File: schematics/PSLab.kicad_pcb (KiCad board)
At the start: 4 copper layers, 99 x 53.3 mm, 182 parts, among them J1 DoublePins, J11 Li-Ion Battery, J2 Power Pins, J3 Wave Generator, J4 I2C, J5 I2C, J6 ESP01, J7 UART, J9 SPI, P1 SDCard, Q1 MMBT3906, Q2 MMBT3904, Q3 MMBT3906, Q4 Q_NMOS_DGS, SW1 BOOT, SW2 MCLR Reset, SW3 USB_C - Generic, U1 LDFM33PUR, U10 TL082, U11 TL082, U12 MCP4728, U13 MCP6S21, U14 MCP6S21, U15 CP2102N, U16 SP0503BAHT, U18 LTC4040, U19 TC1240A, U2 74HC126, U3 PIC24EP256GP204, U4 DS1307Z+, U5 TC7660, U7 LM324, U8 TL082, U9 TL082, X2 32.768 kHz, Y1 12 MHz

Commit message: fix: osc signal routes
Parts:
- BT1: footprint Battery:BatteryHolder_LINX_BAT-HLD-012-SMT -> PSLab:BatteryHolder_LINX_BAT-HLD-012-SMT
- moved TP3 36.7 mm to (145.4, 66.3)
- moved TP2 35.6 mm to (148.7, 66.3)
- moved TP5 35.2 mm to (147.1, 68.6)
- moved TP1 30.4 mm to (152.2, 66.3)
- moved R24 19.9 mm to (180.4, 83.5)
- moved C25 16.0 mm to (180.4, 85.8), turned to 180 degrees
- moved U4 1.46 mm to (158.9, 104.9)
- moved X2 1.28 mm to (165.4, 107.0)
- moved R36 1.09 mm to (176.0, 83.5)
- moved C39 0.99 mm to (180.4, 94.0), turned to 180 degrees
- moved U13 0.95 mm to (178.2, 89.9)
- moved R22 0.78 mm to (176.0, 94.0), turned to 180 degrees
- moved R7 0.77 mm to (180.4, 98.3)
- moved R23 0.75 mm to (176.0, 85.8)
- moved R8 0.72 mm to (180.4, 96.2)
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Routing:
- net AVdd: track 109.0 -> 92.0 mm
- net AVSS: track 304.5 -> 290.5 mm, vias 29 -> 25
- net ACH1: track 12.0 -> 20.4 mm
- net CH1: track 17.6 -> 24.6 mm
- net Net-(BT1-Pad1): track 4.03 -> 1.91 mm
- net VDDA: track 6.73 -> 8.13 mm, vias 1 -> 0
- net LA4: track 8.02 -> 9.34 mm
- net CS.CH1: track 57.0 -> 57.9 mm
- net +5V: track 180.3 -> 179.5 mm, vias 10 -> 9
- net /LA2_: track 50.2 -> 51.0 mm
- net LA3: track 3.15 -> 3.84 mm
- net LA1: track 9.17 -> 9.78 mm
- net /LA3_: track 46.6 -> 47.2 mm
- net LA2: track 3.17 -> 3.68 mm

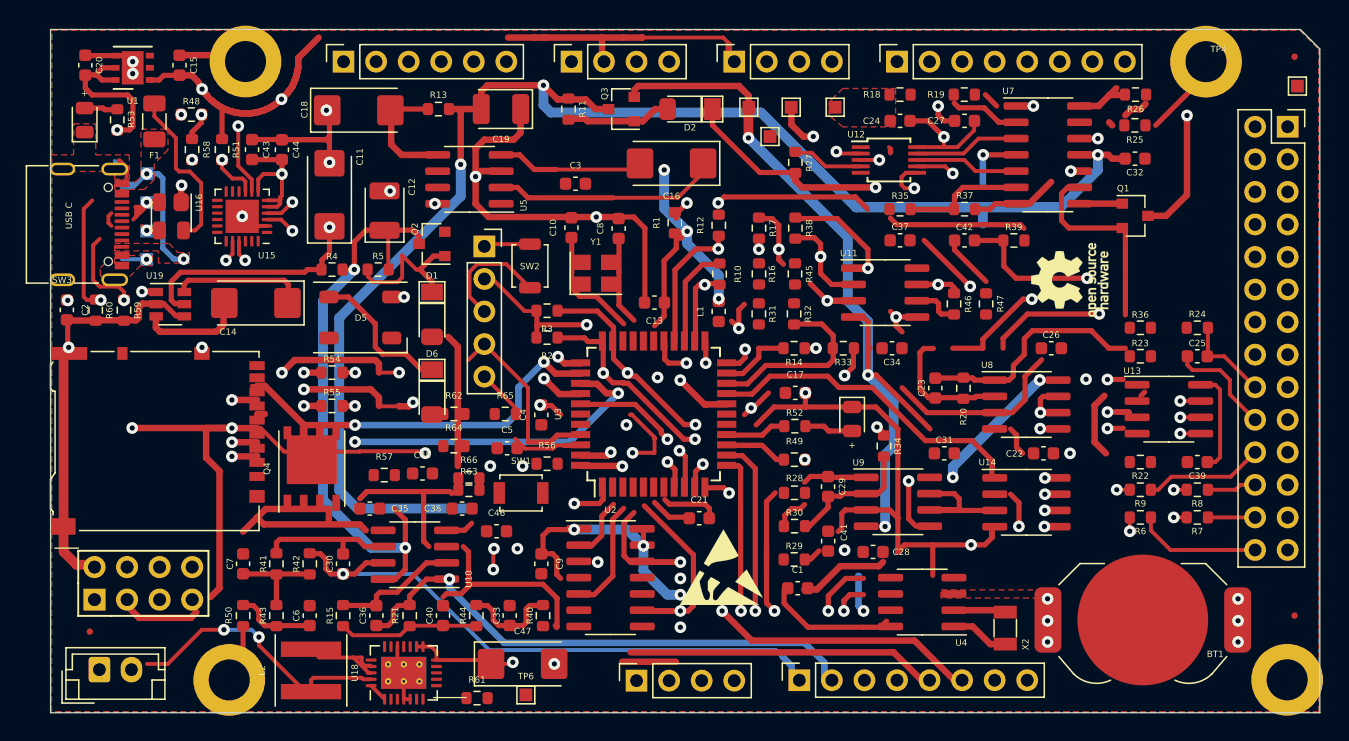
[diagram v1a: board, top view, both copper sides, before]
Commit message: refactor: global track refresh
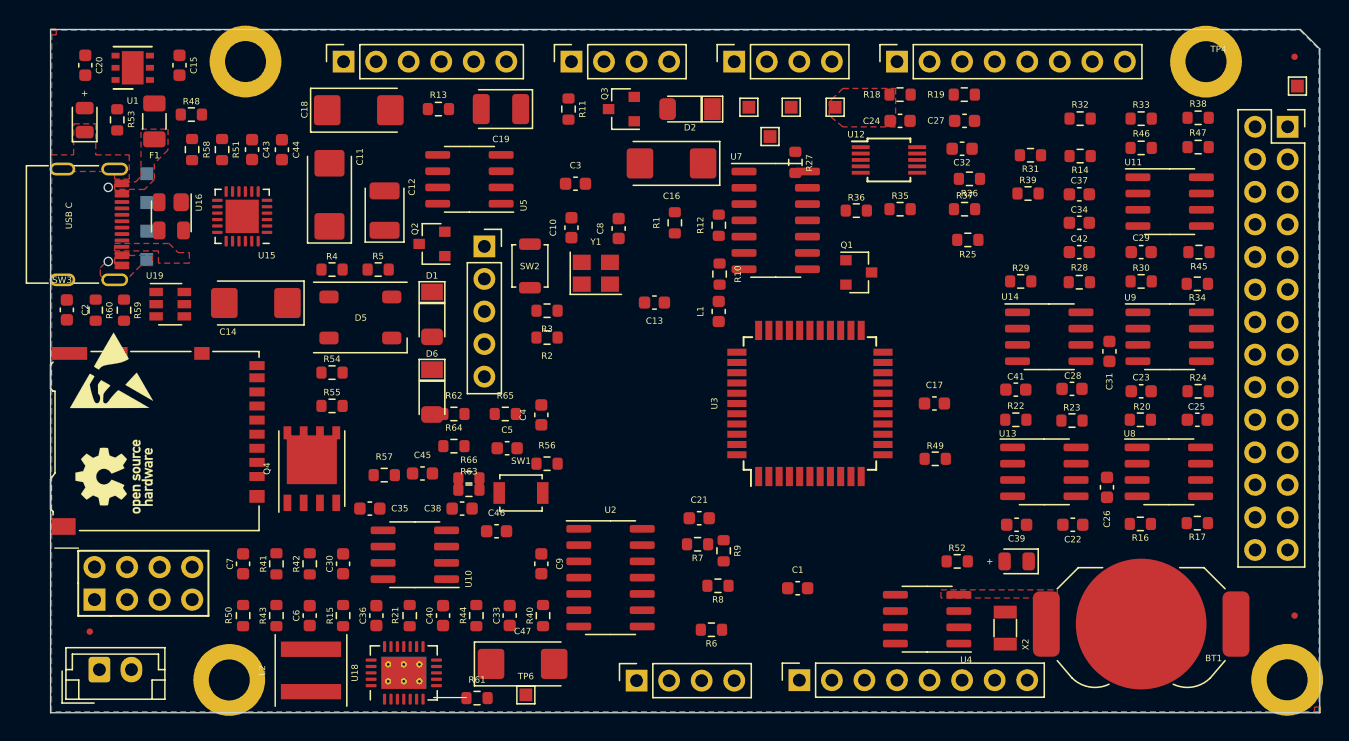
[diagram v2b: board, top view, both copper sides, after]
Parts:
- U1: footprint Package_DFN_QFN:DFN-6-1EP_3x3mm_P0.95mm_EP1.7x2.6mm -> PSLab:DFN-6-1EP_3x3mm_P0.95mm_EP1.7x2.6mm
- moved Z11 76.1 mm to (95.9, 95.2)
- moved Z10 50.0 mm to (95.7, 86.8)
- moved Z8 45.0 mm to (99.8, 92.6)
- moved R17 41.2 mm to (180.4, 98.8), turned to 0 degrees
- moved R7 39.0 mm to (141.4, 100.4)
- moved R8 38.1 mm to (143.0, 103.7)
- moved R16 35.6 mm to (176.0, 98.8), turned to 180 degrees
- moved R6 34.6 mm to (142.5, 107.1)
- moved R30 33.1 mm to (176.0, 79.9)
- moved R9 32.9 mm to (143.5, 100.9), turned to 270 degrees
- moved R38 32.6 mm to (180.5, 67.2), turned to 180 degrees
- moved R45 31.6 mm to (180.5, 77.6), turned to 0 degrees
- moved C29 30.5 mm to (176.0, 77.6), turned to 0 degrees
- moved R33 29.3 mm to (176.0, 67.2)
- moved R29 28.0 mm to (166.6, 79.9)
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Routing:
- net AVSS: track 290.5 -> 0.00 mm, vias 25 -> 0
- net +3V3: track 259.5 -> 0.00 mm, vias 12 -> 0
- net +5V: track 179.5 -> 0.00 mm, vias 9 -> 0
- net -10V: track 134.3 -> 0.00 mm, vias 3 -> 0
- net SDO: track 125.5 -> 0.00 mm, vias 4 -> 0
- net +10V: track 115.8 -> 0.00 mm, vias 4 -> 0
- net SCK: track 111.3 -> 0.00 mm, vias 4 -> 0
- net SDA: track 102.6 -> 0.00 mm, vias 4 -> 0
- net SCL: track 94.7 -> 0.00 mm, vias 4 -> 0
- net AVdd: track 92.0 -> 0.00 mm, vias 6 -> 0
- net +6V: track 83.2 -> 0.00 mm, vias 4 -> 0
- net PGD2: track 65.2 -> 0.00 mm, vias 3 -> 0
- net GND: track 60.9 -> 0.00 mm
- net PGC2: track 60.1 -> 0.00 mm, vias 2 -> 0
- net -6V: track 60.0 -> 0.00 mm, vias 3 -> 0
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- added copper zone on F.Cu, net (none)
- removed copper zone on F.Cu, net STAT

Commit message: upgrade: lm324 to tssop14
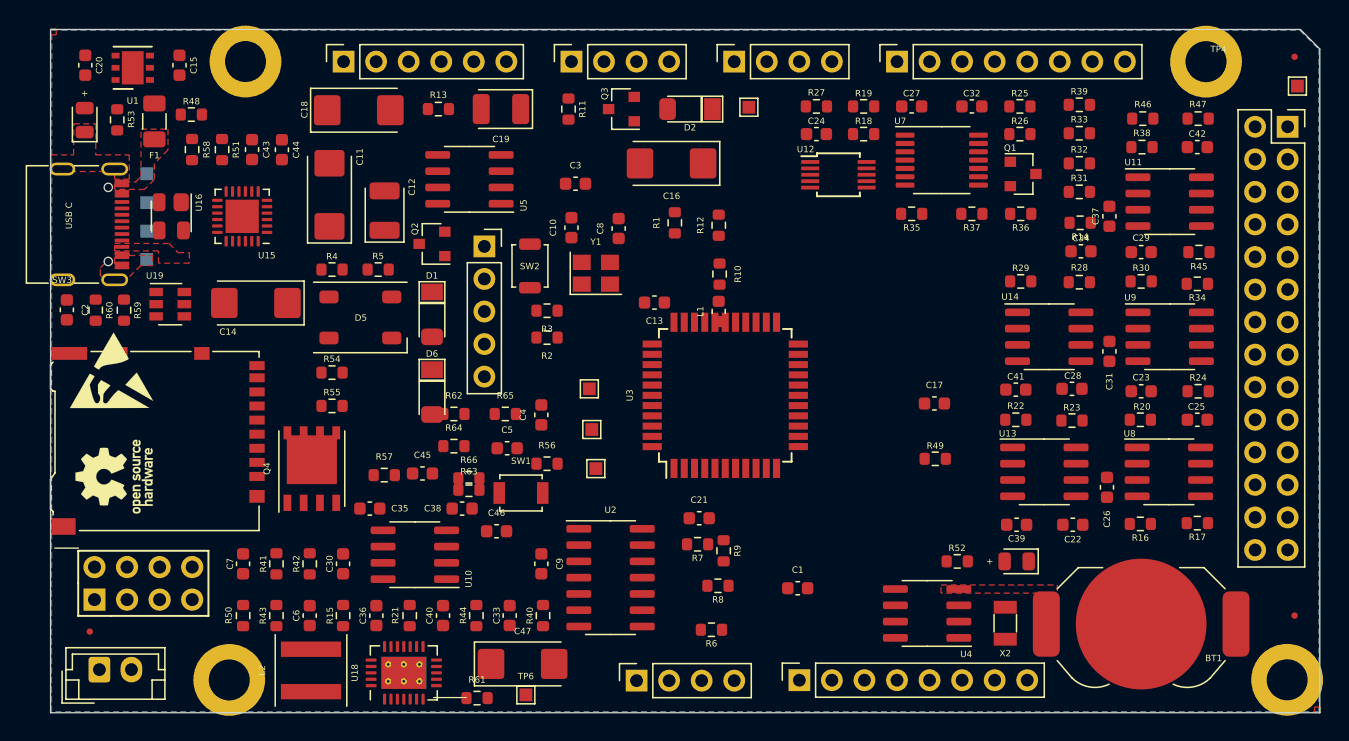
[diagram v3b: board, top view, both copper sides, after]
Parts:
- U7: footprint Package_SO:SOIC-14_3.9x8.7mm_P1.27mm -> Package_SO:TSSOP-14_4.4x5mm_P0.65mm
- moved TP2 32.0 mm to (133.5, 94.5)
- moved TP1 31.5 mm to (133.2, 91.5)
- moved TP5 24.2 mm to (133.0, 88.3)
- moved Q1 15.0 mm to (166.8, 71.5)
- moved U7 13.8 mm to (160.5, 70.5)
- moved R36 12.8 mm to (166.6, 74.7)
- moved C42 12.3 mm to (180.4, 69.4)
- moved R25 11.2 mm to (166.6, 66.3)
- moved R39 7.99 mm to (171.2, 66.1)
- moved R19 7.91 mm to (154.4, 66.3)
- moved U3 6.63 mm to (143.6, 88.8)
- moved C24 6.61 mm to (150.7, 68.4), turned to 0 degrees
- moved R26 5.26 mm to (166.6, 68.4)
- moved R14 5.21 mm to (171.3, 75.4)
- moved R33 4.96 mm to (171.2, 68.4)
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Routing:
- removed copper zone on F.Cu, net AVdd

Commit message: refactor: osc placement
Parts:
- U2: footprint Package_SO:SOIC-14_3.9x8.7mm_P1.27mm -> Package_SO:TSSOP-14_4.4x5mm_P0.65mm
- moved SW2 31.5 mm to (154.2, 96.7)
- moved C3 30.5 mm to (154.3, 92.9), turned to 180 degrees
- moved R12 23.6 mm to (166.6, 77.4), turned to 180 degrees
- moved U2 13.7 mm to (148.2, 105.3)
- moved C10 11.2 mm to (142.7, 74.7)
- moved R6 9.98 mm to (145.9, 97.7), turned to 90 degrees
- moved R8 8.90 mm to (149.6, 97.6), turned to 90 degrees
- moved R9 8.54 mm to (151.3, 97.6), turned to 90 degrees
- moved C1 8.33 mm to (157.3, 101.8)
- moved Y1 8.01 mm to (141.4, 78.2), turned to 180 degrees
- moved R10 7.81 mm to (150.9, 78.3)
- moved R1 7.45 mm to (146.5, 78.3), turned to 270 degrees
- moved C13 7.30 mm to (144.6, 78.3), turned to 90 degrees
- moved L1 6.87 mm to (148.7, 78.3)
- moved R7 6.85 mm to (147.7, 97.7), turned to 90 degrees
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
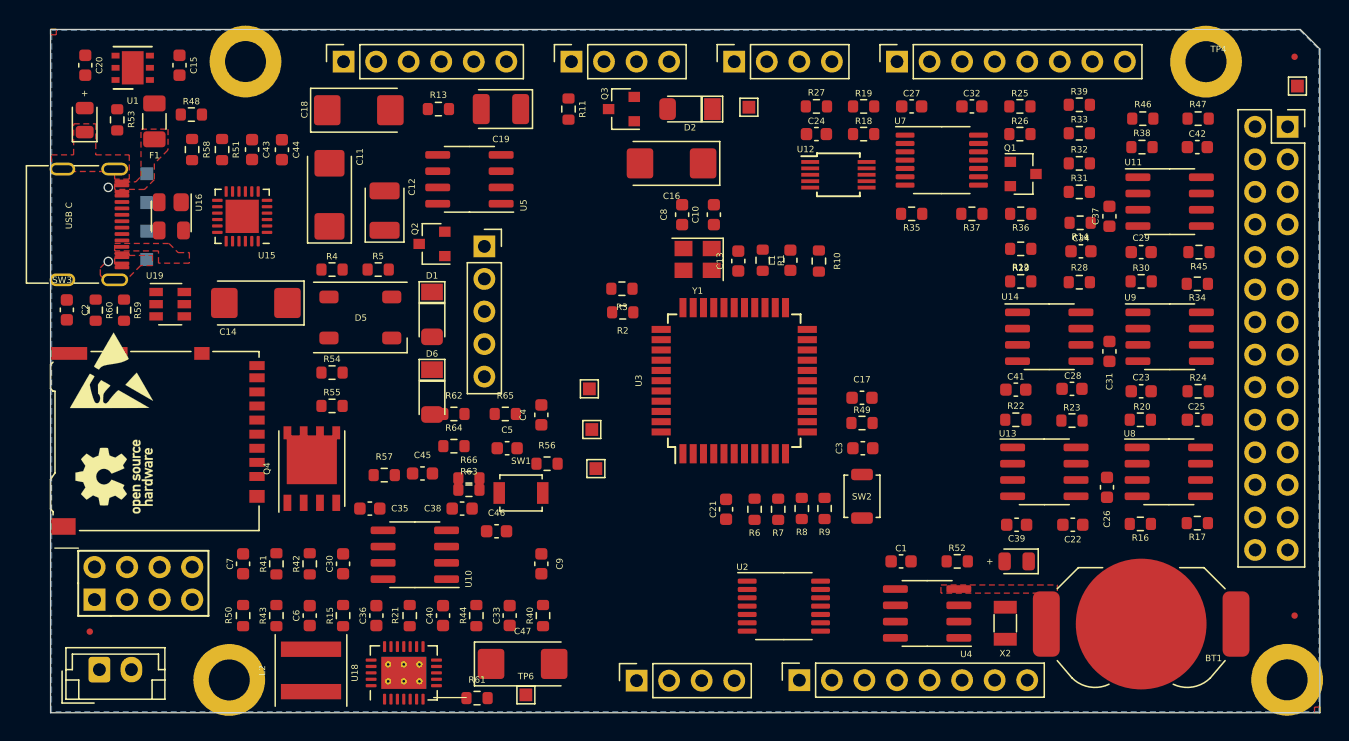
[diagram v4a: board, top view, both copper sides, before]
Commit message: refactor: wave generator circuit
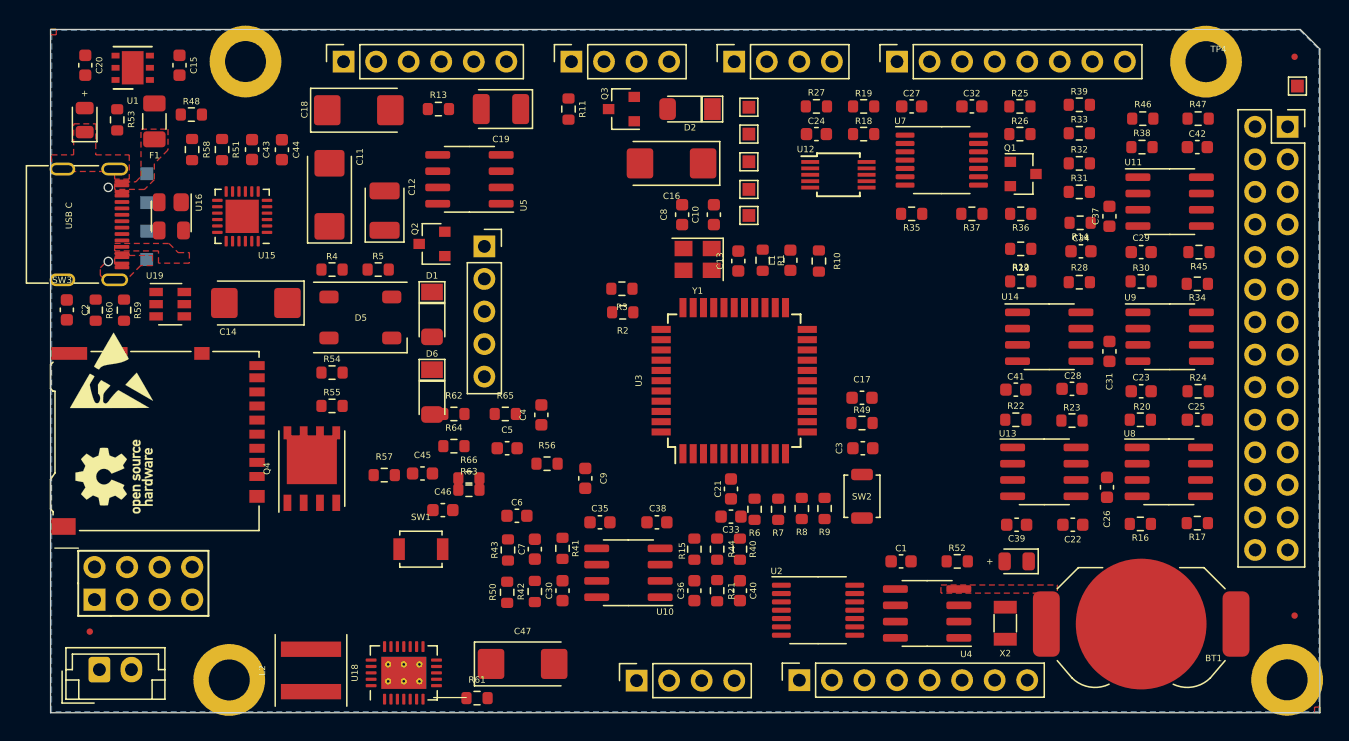
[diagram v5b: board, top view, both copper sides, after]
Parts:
- moved TP6 41.3 mm to (145.4, 74.8)
- moved R15 27.9 mm to (141.2, 100.8), turned to 270 degrees
- moved C36 24.9 mm to (141.2, 104.1)
- moved TP2 24.8 mm to (145.4, 72.7)
- moved TP1 24.2 mm to (145.4, 70.6)
- moved R21 24.1 mm to (142.9, 104.1), turned to 270 degrees
- moved TP5 23.5 mm to (145.4, 68.4)
- moved C40 23.2 mm to (144.7, 104.1), turned to 270 degrees
- moved C7 22.8 mm to (128.7, 100.8)
- moved R41 22.4 mm to (130.9, 100.8), turned to 270 degrees
- moved R50 20.7 mm to (126.6, 104.2)
- moved R44 19.5 mm to (142.9, 100.8)
- moved C33 18.9 mm to (144.0, 98.3), turned to 0 degrees
- moved R43 18.8 mm to (126.6, 100.9)
- moved C35 18.0 mm to (133.8, 98.7), turned to 180 degrees
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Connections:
- U2 pad 2: /SQR1_ -> /SQR2_
- U2 pad 3: SQR1 -> SQR2
- U2 pad 5: /SQR2_ -> /SQR1_
- U2 pad 6: SQR2 -> SQR1
